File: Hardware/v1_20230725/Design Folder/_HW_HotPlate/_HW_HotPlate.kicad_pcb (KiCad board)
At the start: 4 copper layers, 49.7 x 49.7 mm, 129 parts, among them J1001 MICRO B USB_RA, J301 MHDR_4POS_2.54MM_RA, J401 RCPT_2POS_2.54MM_VERT, J501 TERM_3POS_5.08MM_SIDE, J502 TERM_3POS_5.08MM_SIDE, J601 RCPT_8POS_2ROW_2.54MM_RA, J701 RCPT_5POS_2.54MM_RA, J801 RCPT_2POS_2.54MM_VERT, J901 RCPT_2POS_2.54MM_VERT, J902 RCPT_2POS_2.54MM_VERT, J903 RCPT_2POS_2.54MM_VERT, Q501 T2050H-6G-TR, Q801 AS3400, Q901 AS3400, Q902 AS3400, Q903 AS3400, U1001 DLPT05A-7, U1002 DLPT05A-7, U1101 MIC5528-3.3YMT-TR, U1102 MIC5528-3.3YMT-TR, U301 PIC18F24J50-I/ML, U302 SN74LVC1G17DBVR, U303 SN74LVC1G17DBVR, U401 MAX31855JASA+T, U501 140817143400, U502 MOC3022S, U701 SN74LVC1G17DBVR, U702 SN74LVC1G17DBVR, U703 DLPT05A-7, U704 SN74LVC1G17DBVR, X301 16MHz/10ppm

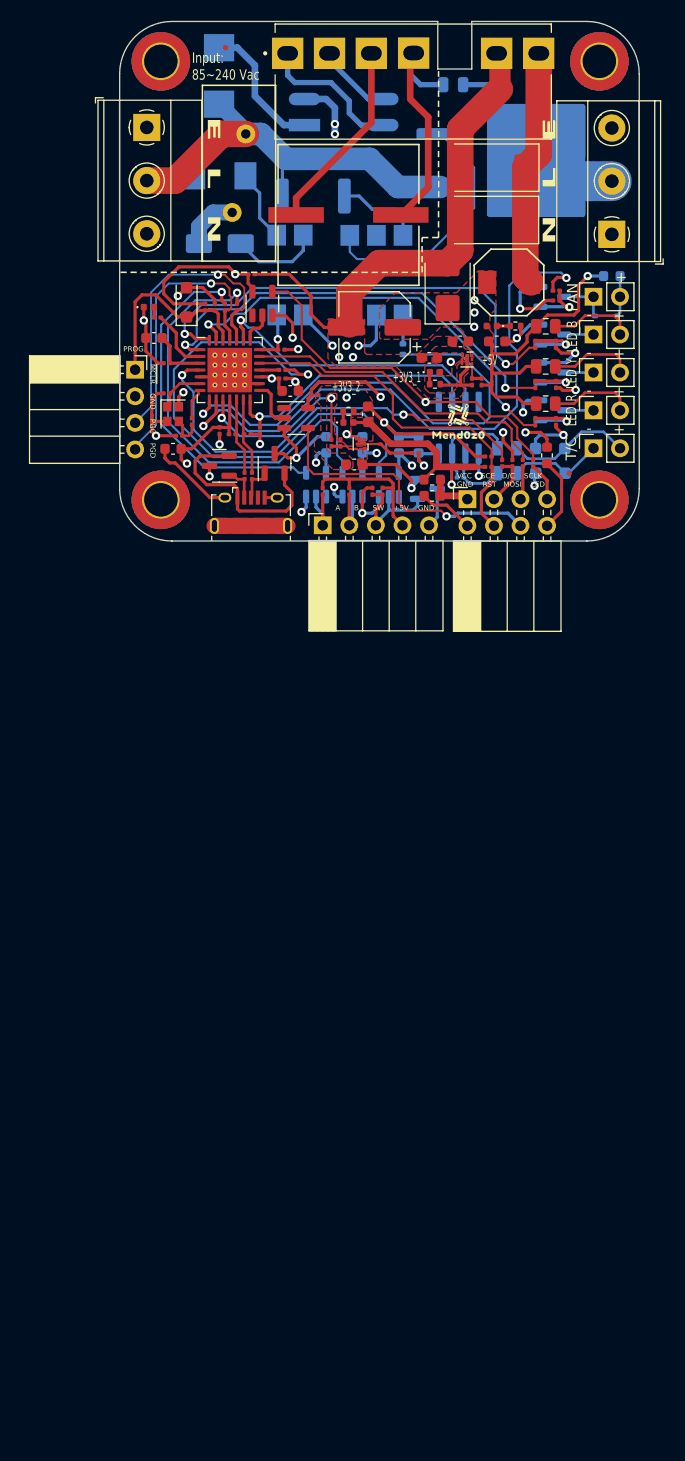
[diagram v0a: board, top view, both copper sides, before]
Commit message: Schematic library has been updated
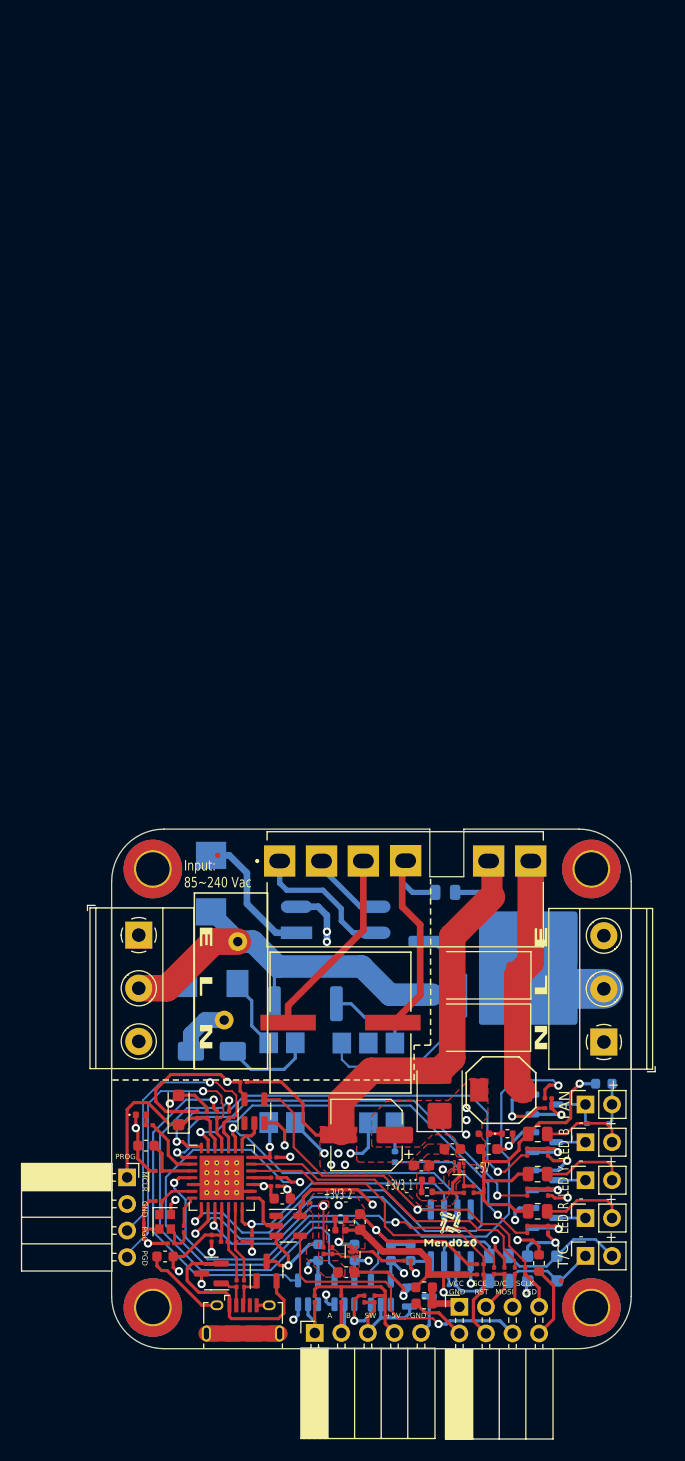
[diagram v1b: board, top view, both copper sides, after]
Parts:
- moved C1102 77.2 mm to (146.6, 210.2)
- moved C302 77.2 mm to (120.4, 243.8)
- moved C305 77.2 mm to (118.0, 234.4)
- moved C310 77.2 mm to (119.8, 245.0)
- moved C311 77.2 mm to (127.3, 228.3)
- moved C402 77.2 mm to (143.3, 244.7)
- moved C403 77.2 mm to (142.9, 245.4)
- moved C701 77.2 mm to (134.4, 244.7)
- moved C702 77.2 mm to (137.9, 244.7)
- moved C703 77.2 mm to (138.8, 249.1)
- moved C704 77.2 mm to (141.4, 244.7)
- moved D501 77.2 mm to (124.3, 225.4)
- moved EC1102 77.2 mm to (136.5, 222.7)
- moved J301 77.2 mm to (116.2, 237.5)
- moved J801 77.2 mm to (160.0, 230.5)
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
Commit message: Updating hardware format structure
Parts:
- C1101: value 100nF/50V -> 100nF_50V_X7R
- C1103, C1104, C1105, C1106, C305, C307, C310, C402, C601, C701, C702, C704: value 10uF/16V -> 10uF_16V_X5R
- C301, C302: value 12pF/50V -> 12pF_50V_C0G
- C303, C304, C306, C308, C309, C311, C403, C602, C703: value 100nF/6V3 -> 100nF_6V3_X7R
- D1101: value SMBJ7.0A -> SMBJ7.0A_7V_50A
- D301, D401, D402: value SMF3.3 -> SMF3.3_3.3V_30A
- D801: value BAT60JFILM -> BAT60JFILM_10V_3A
- EC1101: value 100uF/35V -> 100uF_35V_20%
- EC1102: value 10uF/400V -> 10uF_400V_20%
- J1001: value MICRO B USB_RA -> USB_MICRO B_RA; footprint Connector_USB:USB_Micro-B_Amphenol_10118194_Horizontal -> _PCBLIB_HotPlate:USB_Micro-B_Amphenol_10118194_Horizontal
- J301: value MHDR_4POS_2.54MM_RA -> MHDR_4X1_RA_2.54MM
- J401, J801, J901, J902, J903: value RCPT_2POS_2.54MM_VERT -> RECEPT_2X1_VERT_2.54MM
- J501, J502: value TERM_3POS_5.08MM_SIDE -> TERM_3POS_SIDE_5.08MM
- J601: value RCPT_8POS_2ROW_2.54MM_RA -> RECEPT_4X2_RA_2.54MM
- J701: value RCPT_5POS_2.54MM_RA -> RECEPT_5X1_RA_2.54MM
- L1101: value 50475C -> 4m7H_0.4A
- LED1101: value GREEN -> GREEN_2V8_0.02A
- LED1102, LED1103: value AMBER -> AMBER_2V_0.02A
- LED301: value RED -> RED_2V_0.02A
- Q501: value T2050H-6G-TR -> T2050H-6G-TR_600V_20A
- Q801, Q901, Q902, Q903: footprint Package_TO_SOT_SMD:SOT-23-3 -> Package_TO_SOT_SMD:SOT-23
- R1001, R1002: value 1K5R_1/20W -> 1K5R_1/20W_1%
- R1003, R1004, R301, R605: value 49R9_1/20W -> 49R9_1/20W_1%
- R1101: value 15R_2W -> 15R_2W_5%
- R1102, R1105, R1108, R504: value 330R_1/10W -> 330R_1/10W_1%
- R1103, R1104, R1107, R302, R401, R501, R601, R602, R701, R703, R705, R802, R907, R908, R909: value 10KR_1/20W -> 10KR_1/20W_1%
- R1106, R303, R603, R604, R702, R704, R706, R801, R904, R905, R906: value 100R_1/20W -> 100R_1/20W_1%
- R402, R403: value 1R_1/2W -> 1R_1/2W_5%
- R502: value 100KR_1W -> 100KR_1W_1%
- R503: value 3KR_2W -> 3KR_2W_1%
- R901, R902: value 680R_1/8W -> 680R_1/8W_1%
- R903: value 330R_1/8W -> 330R_1/8W_5%
- RT601: value 30mA_30V -> PTC_30mA_30V_6R
- RT602, RT801: value 100mA_15V -> PTC_100mA_15V_0.9A
- RV1101: value B72214P2351K101 -> B72214P2351K101_350VAC_6kA
- TC1101, TC1102: value 220uF/16V -> 220uF_16V_0.7R
- U1001, U1002, U703: value DLPT05A-7 -> DLPT05A-7_5V_17A
- X301: value 16MHz/10ppm -> 16MHz_10ppm_12pF
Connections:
- net /BLOCK DIAGRAM/FAN DRIVER (12V)/EN_FAN renamed /BLOCK DIAGRAM/FAN DRIVER/EN_FAN
- net /BLOCK DIAGRAM/FAN DRIVER (12V)/FAN_+ renamed /BLOCK DIAGRAM/FAN DRIVER/FAN_+
- net /BLOCK DIAGRAM/FAN DRIVER (12V)/FAN_- renamed /BLOCK DIAGRAM/FAN DRIVER/FAN_-
- net /BLOCK DIAGRAM/ISOLATED TRAIC DRIVER/+3V3_1 renamed /BLOCK DIAGRAM/ISOLATED TRIAC DRIVER/+3V3_1
- net /BLOCK DIAGRAM/ISOLATED TRAIC DRIVER/EN_TRIAC renamed /BLOCK DIAGRAM/ISOLATED TRIAC DRIVER/EN_TRIAC
- net /BLOCK DIAGRAM/ISOLATED TRAIC DRIVER/L_IN renamed /BLOCK DIAGRAM/ISOLATED TRIAC DRIVER/L_IN
- net /BLOCK DIAGRAM/ISOLATED TRAIC DRIVER/L_OUT renamed /BLOCK DIAGRAM/ISOLATED TRIAC DRIVER/L_OUT
- net /BLOCK DIAGRAM/ISOLATED TRAIC DRIVER/MAIN_STROBE renamed /BLOCK DIAGRAM/ISOLATED TRIAC DRIVER/MAIN_STROBE
- net /BLOCK DIAGRAM/ISOLATED TRAIC DRIVER/N renamed /BLOCK DIAGRAM/ISOLATED TRIAC DRIVER/N
- net /BLOCK DIAGRAM/MCU/ENCODER_PB renamed /BLOCK DIAGRAM/MICROCONTROLLER/ENCODER_PB
- net /BLOCK DIAGRAM/MCU/EN_PWR renamed /BLOCK DIAGRAM/MICROCONTROLLER/EN_PWR
- net /BLOCK DIAGRAM/MCU/MAX31855_SO renamed /BLOCK DIAGRAM/MICROCONTROLLER/MAX31855_SO
- net /BLOCK DIAGRAM/MCU/MAX31855_~{CS} renamed /BLOCK DIAGRAM/MICROCONTROLLER/MAX31855_~{CS}
- net /BLOCK DIAGRAM/MCU/PCD8544_D/C renamed /BLOCK DIAGRAM/MICROCONTROLLER/PCD8544_D/C
- net /BLOCK DIAGRAM/MCU/PCD8544_~{CE} renamed /BLOCK DIAGRAM/MICROCONTROLLER/PCD8544_~{CE}
- net /BLOCK DIAGRAM/MCU/PIC18_ICSPPGC renamed /BLOCK DIAGRAM/MICROCONTROLLER/PIC18_ICSPPGC
- net /BLOCK DIAGRAM/MCU/PIC18_ICSPPGD renamed /BLOCK DIAGRAM/MICROCONTROLLER/PIC18_ICSPPGD
- net /BLOCK DIAGRAM/MCU/PIC_OSC1 renamed /BLOCK DIAGRAM/MICROCONTROLLER/PIC_OSC1
- net /BLOCK DIAGRAM/MCU/PIC_OSC2 renamed /BLOCK DIAGRAM/MICROCONTROLLER/PIC_OSC2
- net /BLOCK DIAGRAM/MCU/PIC_SCK1 renamed /BLOCK DIAGRAM/MICROCONTROLLER/PIC_SCK1
- net /BLOCK DIAGRAM/MCU/PIC_SDO1 renamed /BLOCK DIAGRAM/MICROCONTROLLER/PIC_SDO1
- net /BLOCK DIAGRAM/MCU/PIC_VDDCORE renamed /BLOCK DIAGRAM/MICROCONTROLLER/PIC_VDDCORE
- net /BLOCK DIAGRAM/MCU/PIC_~{MCLR} renamed /BLOCK DIAGRAM/MICROCONTROLLER/PIC_~{MCLR}
- net /BLOCK DIAGRAM/MCU/SPI_SCK renamed /BLOCK DIAGRAM/MICROCONTROLLER/SPI_SCK
- net /BLOCK DIAGRAM/MCU/USB_DM renamed /BLOCK DIAGRAM/MICROCONTROLLER/USB_DM
- net /BLOCK DIAGRAM/MCU/USB_DP renamed /BLOCK DIAGRAM/MICROCONTROLLER/USB_DP
- net /BLOCK DIAGRAM/PWR /LS05_+VCAP renamed /BLOCK DIAGRAM/POWER SUPPLY/LS05_+VCAP
- net /BLOCK DIAGRAM/PWR /LS05_-VCAP renamed /BLOCK DIAGRAM/POWER SUPPLY/LS05_-VCAP
- net /BLOCK DIAGRAM/PWR /LS05_ACL renamed /BLOCK DIAGRAM/POWER SUPPLY/LS05_ACL
- net /BLOCK DIAGRAM/PWR /LS05_ACN renamed /BLOCK DIAGRAM/POWER SUPPLY/LS05_ACN
- net /BLOCK DIAGRAM/PWR /MIC5528_EN_1 renamed /BLOCK DIAGRAM/POWER SUPPLY/MIC5528_EN_1
- net /BLOCK DIAGRAM/PWR /MIC5528_EN_2 renamed /BLOCK DIAGRAM/POWER SUPPLY/MIC5528_EN_2
